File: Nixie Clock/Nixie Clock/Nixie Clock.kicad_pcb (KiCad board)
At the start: 2 copper layers, 4 parts, among them Q1 MPSA55, U1 MC34063AP

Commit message: More Nixie Stuff
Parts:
- added J1: PJ-202A, digikey-footprints:Barrel_Jack_5.5mmODx2.1mmID_PJ-202A, F.Cu at (107.2, 76.5)
- added S1: PEC11R-4215F-S0024, digikey-footprints:Rotary_Encoder_Switched_PEC11R, F.Cu at (112.5, 127.8)
- added SW1: 1825910-2, 1825910-2:TE_1825910-2, F.Cu at (83.9, 141.4)
- added U10: PIC16F15325-I/P, Package_DIP:DIP-14_W7.62mm, F.Cu at (159.0, 134.0)
- added U2: MC34063AP, Package_DIP:DIP-8_W7.62mm, F.Cu at (112.6, 91.6)
- added U3: IRF630, IRF630:TO220V, F.Cu at (95.8, 102.4)
- added U4: TPIC6595N, TPIC6595N:DIP254P762X508-20, F.Cu at (73.7, 102.4)
- added U5: TPIC6595N, TPIC6595N:DIP254P762X508-20, F.Cu at (53.1, 102.4)
- added U6: TPIC6595N, TPIC6595N:DIP254P762X508-20, F.Cu at (42.8, 102.4)
- added U7: TPIC6595N, TPIC6595N:DIP254P762X508-20, F.Cu at (84.0, 102.4)
- added U8: TPIC6595N, TPIC6595N:DIP254P762X508-20, F.Cu at (63.4, 102.4)
- added U9: TPIC6595N, TPIC6595N:DIP254P762X508-20, F.Cu at (72.7, 141.9)
- U1: value MC34063AP -> LM1086IT-5.0; footprint Package_DIP:DIP-8_W7.62mm -> LM1086IT-5:TO254P1054X470X1955-3
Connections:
- D1 pad 1: unconnected-(D1-Pad1) -> Net-(D1-Pad1)
- D1 pad 2: unconnected-(D1-Pad2) -> Net-(D1-Pad2)
- D2 pad 1: unconnected-(D2-Pad1) -> VDC
- D2 pad 2: unconnected-(D2-Pad2) -> Net-(D2-Pad2)
- Q1 pad 1: unconnected-(Q1-Pad1) -> Net-(D1-Pad1)
- Q1 pad 2: unconnected-(Q1-Pad2) -> Net-(D1-Pad2)
- Q1 pad 3: unconnected-(Q1-Pad3) -> GND

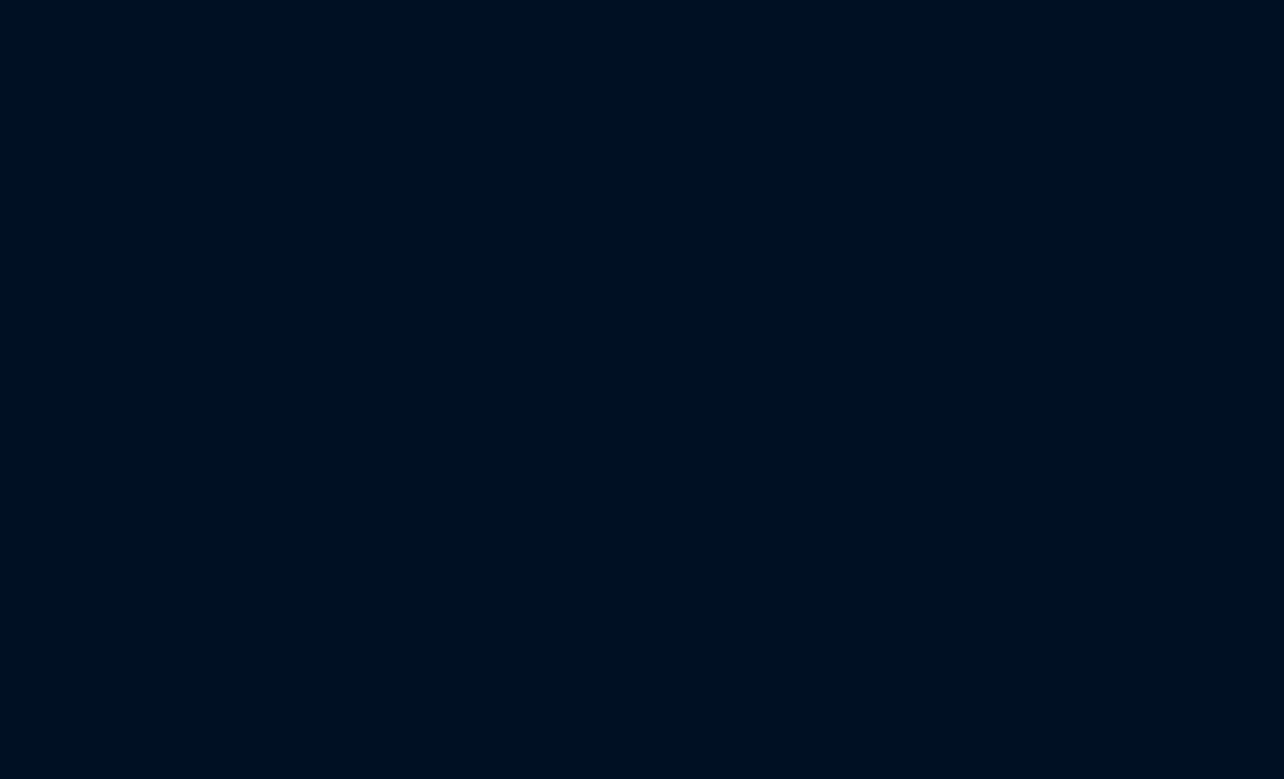
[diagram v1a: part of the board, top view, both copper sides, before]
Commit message: Need to add footprints for passives
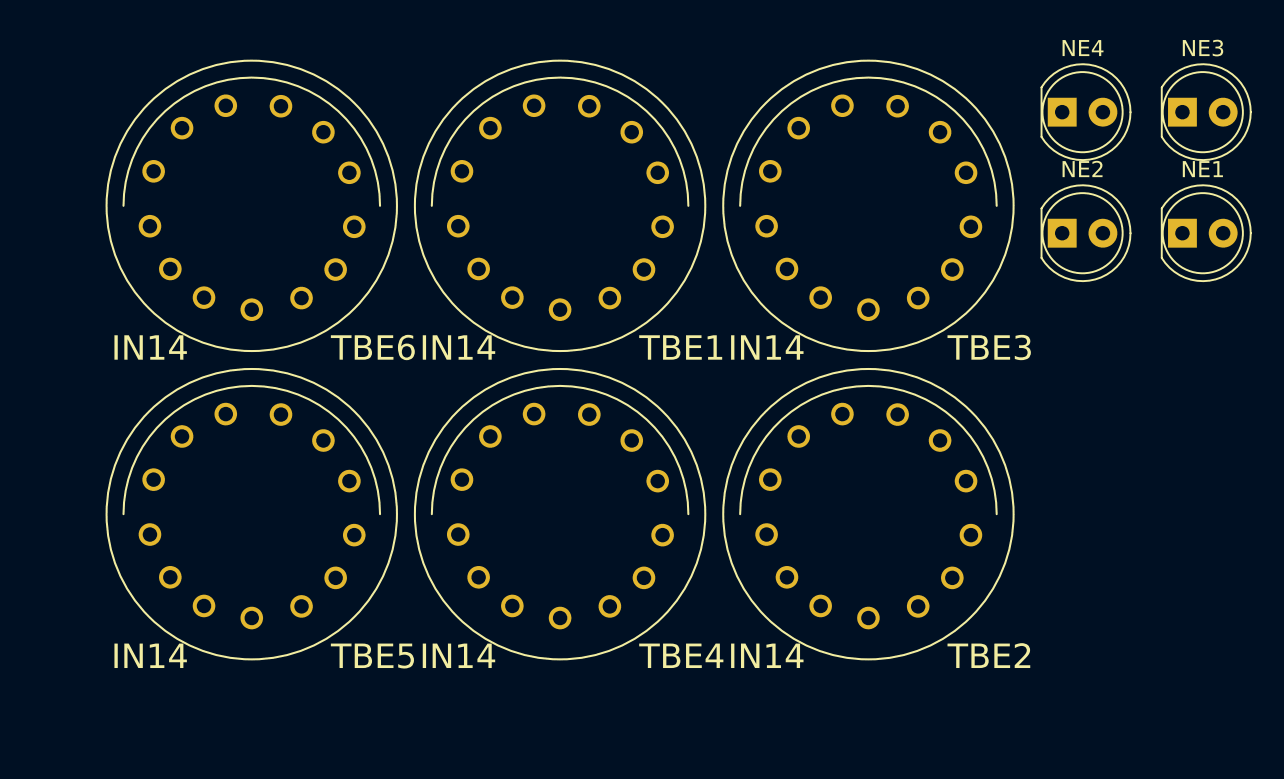
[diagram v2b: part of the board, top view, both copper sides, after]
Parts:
- added NE1: Lamp_Neon, LED_THT:LED_D5.0mm_Clear, F.Cu at (251.0, 53.0)
- added NE2: Lamp_Neon, LED_THT:LED_D5.0mm_Clear, F.Cu at (243.5, 53.0)
- added NE3: Lamp_Neon, LED_THT:LED_D5.0mm_Clear, F.Cu at (251.0, 45.5)
- added NE4: Lamp_Neon, LED_THT:LED_D5.0mm_Clear, F.Cu at (243.5, 45.5)
- added TBE1: IN14, tlnixie-master:IN-14-mod, F.Cu at (212.2, 51.3)
- added TBE2: IN14, tlnixie-master:IN-14-mod, F.Cu at (231.4, 70.5)
- added TBE3: IN14, tlnixie-master:IN-14-mod, F.Cu at (231.4, 51.3)
- added TBE4: IN14, tlnixie-master:IN-14-mod, F.Cu at (212.2, 70.5)
- added TBE5: IN14, tlnixie-master:IN-14-mod, F.Cu at (193.0, 70.5)
- added TBE6: IN14, tlnixie-master:IN-14-mod, F.Cu at (193.0, 51.3)
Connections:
- U1 pad 1: unconnected-(U1-Pad1) -> GND
- U1 pad 2: unconnected-(U1-Pad2) -> +5V
- U1 pad 3: unconnected-(U1-Pad3) -> +12V
- U9 pad 5: /Shift Registers/Tube_5_Digit_9 -> /Tube_5_Digit_9

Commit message: Started Routing
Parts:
- removed NE3, NE4: Lamp_Neon, LED_THT:LED_D5.0mm_Clear
- added C1: 10uF, Capacitor_THT:CP_Radial_D5.0mm_P2.00mm, F.Cu at (131.1, 57.1)
- added C10: 0.1uF, Capacitor_THT:C_Rect_L7.0mm_W3.5mm_P5.00mm, F.Cu at (147.1, 133.3)
- added C11: 0.1uF, Capacitor_THT:C_Rect_L7.0mm_W3.5mm_P5.00mm, F.Cu at (176.3, 133.4)
- added C12: 0.1uF, Capacitor_THT:C_Rect_L7.0mm_W3.5mm_P5.00mm, F.Cu at (197.9, 133.4)
- added C13: 18pF, Capacitor_THT:C_Rect_L7.0mm_W2.5mm_P5.00mm, F.Cu at (158.7, 58.8)
- added C14: 18pF, Capacitor_THT:C_Rect_L7.0mm_W2.5mm_P5.00mm, F.Cu at (158.7, 63.8)
- added C15: 0.1uF, Capacitor_THT:C_Rect_L7.0mm_W3.5mm_P5.00mm, F.Cu at (173.0, 51.0)
- added C16: 0.01uF, Capacitor_THT:C_Disc_D12.0mm_W4.4mm_P7.75mm, F.Cu at (198.2, 78.4)
- added C17: 0.01uF, Capacitor_THT:C_Disc_D12.0mm_W4.4mm_P7.75mm, F.Cu at (205.7, 78.4)
- added C18: 0.1uF, Capacitor_THT:C_Rect_L7.0mm_W3.5mm_P5.00mm, F.Cu at (191.7, 44.1)
- added C2: 10 uF, Capacitor_THT:CP_Radial_D5.0mm_P2.00mm, F.Cu at (137.3, 57.1)
- added C3: 680pF, Capacitor_THT:C_Disc_D7.5mm_W4.4mm_P5.00mm, F.Cu at (110.2, 52.7)
- added C4: 220uF 25V, Capacitor_THT:CP_Radial_D10.0mm_P5.00mm, F.Cu at (104.7, 74.7)
- added C5: 0.01uF, Capacitor_THT:C_Disc_D12.0mm_W4.4mm_P7.75mm, F.Cu at (116.5, 71.0)
- added C6: 2.2uF 250V, Capacitor_THT:CP_Radial_D6.3mm_P2.50mm, F.Cu at (84.7, 59.7)
- added C7: 0.1uF, Capacitor_THT:C_Rect_L7.0mm_W3.5mm_P5.00mm, F.Cu at (76.0, 133.4)
- added C8: 0.1uF, Capacitor_THT:C_Rect_L7.0mm_W3.5mm_P5.00mm, F.Cu at (97.6, 133.4)
- added C9: 0.1uF, Capacitor_THT:C_Rect_L7.0mm_W3.5mm_P5.00mm, F.Cu at (126.8, 133.4)
- added J2: Conn_01x05_Male, Connector_PinHeader_2.54mm:PinHeader_1x05_P2.54mm_Vertical, F.Cu at (184.9, 57.2)
- added L1: 150uH 1.1A, Inductor_THT:L_Radial_D12.0mm_P10.00mm_Neosid_SD12_style1, F.Cu at (98.7, 74.7)
- added R1: 0.5, Resistor_THT:R_Axial_DIN0207_L6.3mm_D2.5mm_P10.16mm_Horizontal, F.Cu at (125.7, 57.3)
- added R10: 10k, Resistor_THT:R_Axial_DIN0207_L6.3mm_D2.5mm_P10.16mm_Horizontal, F.Cu at (204.5, 72.1)
- added R11: 10k, Resistor_THT:R_Axial_DIN0207_L6.3mm_D2.5mm_P10.16mm_Horizontal, F.Cu at (199.4, 72.1)
- added R12: 10k, Resistor_THT:R_Axial_DIN0207_L6.3mm_D2.5mm_P10.16mm_Horizontal, F.Cu at (209.6, 61.9)
- added R13: 10k, Resistor_THT:R_Axial_DIN0207_L6.3mm_D2.5mm_P10.16mm_Horizontal, F.Cu at (181.6, 50.5)
- added R14: 14k, Resistor_THT:R_Axial_DIN0207_L6.3mm_D2.5mm_P10.16mm_Horizontal, F.Cu at (203.0, 108.0)
- added R15: 14k, Resistor_THT:R_Axial_DIN0207_L6.3mm_D2.5mm_P10.16mm_Horizontal, F.Cu at (131.6, 108.0)
- added R16: 14k, Resistor_THT:R_Axial_DIN0207_L6.3mm_D2.5mm_P10.16mm_Horizontal, F.Cu at (172.5, 100.3)
- added R17: 14k, Resistor_THT:R_Axial_DIN0207_L6.3mm_D2.5mm_P10.16mm_Horizontal, F.Cu at (121.7, 100.3)
- added R2: 0.5, Resistor_THT:R_Axial_DIN0207_L6.3mm_D2.5mm_P10.16mm_Horizontal, F.Cu at (120.7, 57.3)
- added R20: 14k, Resistor_THT:R_Axial_DIN0207_L6.3mm_D2.5mm_P10.16mm_Horizontal, F.Cu at (182.2, 108.0)
- added R21: 14k, Resistor_THT:R_Axial_DIN0207_L6.3mm_D2.5mm_P10.16mm_Horizontal, F.Cu at (101.8, 108.0)
- added R22: 14k, Resistor_THT:R_Axial_DIN0207_L6.3mm_D2.5mm_P10.16mm_Horizontal, F.Cu at (152.4, 108.0)
- added R23: 14k, Resistor_THT:R_Axial_DIN0207_L6.3mm_D2.5mm_P10.16mm_Horizontal, F.Cu at (81.1, 108.0)
- added R3: 1k, Resistor_THT:R_Axial_DIN0207_L6.3mm_D2.5mm_P10.16mm_Horizontal, F.Cu at (106.0, 53.7)
- added R4: 475k 1%, Resistor_THT:R_Axial_DIN0207_L6.3mm_D2.5mm_P10.16mm_Horizontal, F.Cu at (136.6, 80.2)
- added R5: 13.7k 1%, Resistor_THT:R_Axial_DIN0207_L6.3mm_D2.5mm_P10.16mm_Horizontal, F.Cu at (122.3, 70.0)
- added R6: 4.02k 1%, Resistor_THT:R_Axial_DIN0207_L6.3mm_D2.5mm_P10.16mm_Horizontal, F.Cu at (127.1, 80.2)
- added R7: 680 1%, Resistor_THT:R_Axial_DIN0207_L6.3mm_D2.5mm_P10.16mm_Horizontal, F.Cu at (131.8, 80.2)
- added R8: 10k, Resistor_THT:R_Axial_DIN0207_L6.3mm_D2.5mm_P10.16mm_Horizontal, F.Cu at (158.2, 72.3)
- added R9: 10k, Resistor_THT:R_Axial_DIN0207_L6.3mm_D2.5mm_P10.16mm_Horizontal, F.Cu at (194.3, 72.1)
- added REF**: Symbol_Highvoltage_Type1_CopperTop_Small, Symbol:Symbol_Highvoltage_Type1_CopperTop_Small, F.Cu at (80.3, 65.9)
- added Y1: 12.288MHz, Crystal:Crystal_HC49-4H_Vertical, F.Cu at (164.9, 58.9)
- moved U4 142.8 mm to (211.9, 138.4)
- moved U5 142.6 mm to (191.1, 138.4)
- moved NE2 129.2 mm to (120.5, 92.7)
- moved U6 123.8 mm to (161.3, 138.4)
- moved TBE6 114.6 mm to (86.1, 92.7)
- moved S1 114.2 mm to (196.3, 50.2)
- moved SW1 108.8 mm to (175.5, 82.8), turned to 180 degrees
- moved TBE4 107.6 mm to (106.9, 92.7)
- moved TBE2 97.3 mm to (136.7, 92.7)
- moved Q1 90.6 mm to (92.6, 59.9), turned to 90 degrees
- moved NE1 89.2 mm to (171.1, 92.7)
- moved U10 78.2 mm to (171.7, 56.9)
- moved D2 72.4 mm to (84.7, 64.9)
- moved U7 67.0 mm to (140.5, 138.4)
- moved D1 62.3 mm to (97.1, 58.3)
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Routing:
- net VDC: track 0.00 -> 132.4 mm
- net /Shift Clock: track 0.00 -> 127.2 mm
- net /Data Latch: track 0.00 -> 127.2 mm
- net /Tube_5_Digit_5: track 0.00 -> 51.3 mm
- net /Tube_5_Digit_4: track 0.00 -> 49.3 mm
- net /Tube_3_Digit_4: track 0.00 -> 49.3 mm, vias 0 -> 1
- net /Tube_1_Digit_4: track 0.00 -> 48.6 mm
- net /Tube_5_Digit_6: track 0.00 -> 48.3 mm, vias 0 -> 2
- net /Tube_3_Digit_5: track 0.00 -> 47.9 mm, vias 0 -> 1
- net /Tube_1_Digit_3: track 0.00 -> 47.2 mm
- net /Tube_4_Digit_5: track 0.00 -> 47.1 mm, vias 0 -> 1
- net /Tube_1_Digit_5: track 0.00 -> 47.0 mm, vias 0 -> 1
- net /Tube_5_Digit_3: track 0.00 -> 46.4 mm
- net /Tube_3_Digit_8: track 0.00 -> 46.1 mm
- net /Tube_3_Digit_3: track 0.00 -> 46.1 mm
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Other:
- board outline added: 150 x 104 mm

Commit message: Mostly finished Nixie Tube Project
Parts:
- moved C5 12.9 mm to (129.3, 69.7)
- moved D1 12.9 mm to (109.9, 57.0)
- moved J1 12.9 mm to (136.9, 49.6)
- moved R5 12.9 mm to (135.2, 68.7)
- moved R6 12.9 mm to (139.9, 78.9)
- moved C4 12.9 mm to (117.5, 73.4)
- moved U2 12.9 mm to (121.7, 57.2)
- moved C1 12.9 mm to (143.9, 55.8)
- moved C2 12.9 mm to (150.1, 55.8)
- moved C3 12.9 mm to (123.0, 51.4)
- moved C6 12.9 mm to (97.5, 58.4)
- moved Q1 12.9 mm to (105.4, 58.6)
- moved R1 12.9 mm to (138.5, 56.0)
- moved R2 12.9 mm to (133.5, 56.0)
- moved R3 12.9 mm to (118.9, 52.4)
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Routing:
- net +5V: track 38.2 -> 436.4 mm, vias 0 -> 3
- net VDC: track 132.4 -> 248.8 mm
- net /Data Output: track 0.00 -> 87.1 mm, vias 0 -> 1
- net /Shift Clock: track 127.2 -> 206.0 mm, vias 0 -> 1
- net /Data Latch: track 127.2 -> 202.0 mm, vias 0 -> 1
- net Net-(C4-Pad1): track 0.00 -> 47.3 mm
- net /Microcontroller/Encoder B: track 6.85 -> 44.7 mm
- net /Microcontroller/Rotary Button: track 0.00 -> 37.0 mm
- net +12V: track 0.28 -> 28.0 mm
- net Net-(C5-Pad1): track 0.03 -> 26.7 mm
- net /Microcontroller/Encoder A: track 7.98 -> 31.3 mm, vias 0 -> 1
- net Net-(D1-Pad2): track 0.00 -> 23.3 mm
- net Net-(D2-Pad2): track 0.76 -> 21.9 mm
- net Net-(D1-Pad1): track 0.00 -> 12.7 mm
- net Net-(C3-Pad1): track 0.00 -> 12.1 mm
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- added copper zone on B.Cu, net GND
- added copper zone on F.Cu, net GND
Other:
- board text added: "12V 2A Input"
- board text added: "Nixie Tube Clock"
- board text added: "Rotary Knob"
- board text added: "To set hours, push rotary knob and turn. Repeat for minutes and seconds. Push again to start clock."
- board text added: "WARNING! HIGH VOLTAGE!"

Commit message: Nixie
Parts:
- removed J2: Conn_01x05_Male, Connector_PinHeader_2.54mm:PinHeader_1x05_P2.54mm_Vertical
- removed R22, R23: 14k, Resistor_THT:R_Axial_DIN0207_L6.3mm_D2.5mm_P10.16mm_Horizontal
- removed REF**: Symbol_Highvoltage_Type1_CopperTop_Small, Symbol:Symbol_Highvoltage_Type1_CopperTop_Small
- added R18: 14k, Resistor_THT:R_Axial_DIN0204_L3.6mm_D1.6mm_P7.62mm_Horizontal, F.Cu at (243.5, 101.8)
- added R19: 14k, Resistor_THT:R_Axial_DIN0204_L3.6mm_D1.6mm_P7.62mm_Horizontal, F.Cu at (243.5, 98.7)
- C1, C2: footprint Capacitor_THT:CP_Radial_D5.0mm_P2.00mm -> Capacitor_THT:CP_Radial_D6.3mm_P2.50mm
- C10, C11, C12, C15, C18, C7, C8, C9: footprint Capacitor_THT:C_Rect_L7.0mm_W3.5mm_P5.00mm -> Capacitor_THT:CP_Radial_D4.0mm_P1.50mm
- C13, C14: footprint Capacitor_THT:C_Rect_L7.0mm_W2.5mm_P5.00mm -> Capacitor_THT:C_Disc_D5.0mm_W2.5mm_P2.50mm
- C16, C17, C5: footprint Capacitor_THT:C_Disc_D12.0mm_W4.4mm_P7.75mm -> Capacitor_THT:C_Disc_D5.1mm_W3.2mm_P5.00mm
- C3: footprint Capacitor_THT:C_Disc_D7.5mm_W4.4mm_P5.00mm -> Capacitor_THT:C_Disc_D3.8mm_W2.6mm_P2.50mm
- C4: footprint Capacitor_THT:CP_Radial_D10.0mm_P5.00mm -> Capacitor_THT:CP_Radial_D8.0mm_P3.50mm
- L1: footprint Inductor_THT:L_Radial_D12.0mm_P10.00mm_Neosid_SD12_style1 -> Inductor_THT:L_Radial_D21.0mm_P19.00mm
- R1, R2: footprint Resistor_THT:R_Axial_DIN0207_L6.3mm_D2.5mm_P10.16mm_Horizontal -> Resistor_THT:R_Axial_DIN0414_L11.9mm_D4.5mm_P15.24mm_Horizontal
- R10, R11, R12, R13, R8, R9: footprint Resistor_THT:R_Axial_DIN0207_L6.3mm_D2.5mm_P10.16mm_Horizontal -> Resistor_THT:R_Axial_DIN0309_L9.0mm_D3.2mm_P12.70mm_Horizontal
- R14, R15, R20, R21, R4, R6: footprint Resistor_THT:R_Axial_DIN0207_L6.3mm_D2.5mm_P10.16mm_Horizontal -> Resistor_THT:R_Axial_DIN0204_L3.6mm_D1.6mm_P7.62mm_Horizontal
- U3: footprint IRF630:TO220V -> Package_TO_SOT_THT:TO-220-3_Vertical
- moved U3 3.64 mm to (111.0, 62.9)
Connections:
- R11 pad 1: +5V -> Net-(R11-Pad1)
- R11 pad 2: Net-(R11-Pad2) -> +5V
- R12 pad 1: Net-(R10-Pad2) -> +5V
- R12 pad 2: +5V -> Net-(R10-Pad2)
- R13 pad 1: +5V -> /Microcontroller/Rotary Button
- R13 pad 2: /Microcontroller/Rotary Button -> +5V
- R9 pad 2: Net-(R11-Pad2) -> Net-(R11-Pad1)
- S1 pad A: Net-(R11-Pad2) -> Net-(R11-Pad1)
- TBE3 pad 1: Net-(R20-Pad1) -> Net-(R18-Pad1)
- TBE4 pad 1: Net-(R21-Pad1) -> Net-(R19-Pad1)
- TBE5 pad 1: Net-(R22-Pad1) -> Net-(R20-Pad1)
- TBE6 pad 1: Net-(R23-Pad1) -> Net-(R21-Pad1)
- U10 pad 12: /Microcontroller/Program Clock -> unconnected-(U10-Pad12)
- U10 pad 13: /Microcontroller/Program Data -> unconnected-(U10-Pad13)
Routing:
- net +5V: track 436.4 -> 0.00 mm, vias 3 -> 0
- net VDC: track 248.8 -> 0.00 mm
- net /Shift Clock: track 206.0 -> 0.00 mm, vias 1 -> 0
- net /Data Latch: track 202.0 -> 0.00 mm, vias 1 -> 0
- net /Data Output: track 87.1 -> 0.00 mm, vias 1 -> 0
- net /Tube_5_Digit_5: track 51.3 -> 0.00 mm
- net /Tube_5_Digit_4: track 49.3 -> 0.00 mm
- net /Tube_3_Digit_4: track 49.3 -> 0.00 mm, vias 1 -> 0
- net /Tube_1_Digit_4: track 48.6 -> 0.00 mm
- net /Tube_5_Digit_6: track 48.3 -> 0.00 mm, vias 2 -> 0
- net /Tube_3_Digit_5: track 47.9 -> 0.00 mm, vias 1 -> 0
- net Net-(C4-Pad1): track 47.3 -> 0.00 mm
- net /Tube_1_Digit_3: track 47.2 -> 0.00 mm
- net /Tube_4_Digit_5: track 47.1 -> 0.00 mm, vias 1 -> 0
- net /Tube_1_Digit_5: track 47.0 -> 0.00 mm, vias 1 -> 0
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- removed copper zone on B.Cu, net GND
- removed copper zone on F.Cu, net GND
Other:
- board outline removed

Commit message: Added additional parts
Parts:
- added D3: LED_RGB, CLY6D-FKC-CK1N1D1BB7D3D3:CLY6D-FKC-CK1N1D1BB7D3D3, F.Cu at (93.2, 107.3)
- added D4: LED_RGB, CLY6D-FKC-CK1N1D1BB7D3D3:CLY6D-FKC-CK1N1D1BB7D3D3, F.Cu at (113.9, 107.3)
- added D5: LED_RGB, CLY6D-FKC-CK1N1D1BB7D3D3:CLY6D-FKC-CK1N1D1BB7D3D3, F.Cu at (141.8, 107.3)
- added D6: LED_RGB, CLY6D-FKC-CK1N1D1BB7D3D3:CLY6D-FKC-CK1N1D1BB7D3D3, F.Cu at (162.6, 107.3)
- added D7: LED_RGB, CLY6D-FKC-CK1N1D1BB7D3D3:CLY6D-FKC-CK1N1D1BB7D3D3, F.Cu at (190.5, 107.3)
- added D8: LED_RGB, CLY6D-FKC-CK1N1D1BB7D3D3:CLY6D-FKC-CK1N1D1BB7D3D3, F.Cu at (211.2, 107.3)
- added H1: MountingHole, MountingHole:MountingHole_4.3mm_M4, F.Cu at (220.8, 50.0)
- added H2: MountingHole, MountingHole:MountingHole_4.3mm_M4, F.Cu at (80.0, 50.0)
- added H3: MountingHole, MountingHole:MountingHole_4.3mm_M4, F.Cu at (221.2, 147.5)
- added H4: MountingHole, MountingHole:MountingHole_4.3mm_M4, F.Cu at (80.0, 147.5)
- added R22: Resistor_THT:R_Axial_DIN0207_L6.3mm_D2.5mm_P10.16mm_Horizon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, Resistor_THT:R_Axial_DIN0207_L6.3mm_D2.5mm_P10.16mm_Horizontal, F.Cu at (81.0, 101.9)
- added R23: 110, Resistor_THT:R_Axial_DIN0411_L9.9mm_D3.6mm_P12.70mm_Horizontal, F.Cu at (102.3, 81.0)
- added R24: Resistor_THT:R_Axial_DIN0207_L6.3mm_D2.5mm_P10.16mm_Horizon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, Resistor_THT:R_Axial_DIN0207_L6.3mm_D2.5mm_P10.16mm_Horizontal, F.Cu at (81.0, 128.0)
- added R25: 150, Resistor_THT:R_Axial_DIN0414_L11.9mm_D4.5mm_P15.24mm_Horizontal, F.Cu at (104.6, 94.0)
- added R26: Resistor_THT:R_Axial_DIN0207_L6.3mm_D2.5mm_P10.16mm_Horizon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, Resistor_THT:R_Axial_DIN0207_L6.3mm_D2.5mm_P10.16mm_Horizontal, F.Cu at (81.0, 114.9)
- added R27: 150, Resistor_THT:R_Axial_DIN0414_L11.9mm_D4.5mm_P15.24mm_Horizontal, F.Cu at (104.6, 87.0)
- added RV1: 10K, WH148:WH148, F.Cu at (81.0, 61.2)
- added RV2: 10K, WH148:WH148, F.Cu at (81.0, 93.2)
- added RV3: 10K, WH148:WH148, F.Cu at (81.0, 77.2)
- Q1: footprint MPSA55:TO92127P520H787-3 -> Package_TO_SOT_THT:TO-92_Inline
- moved R19 128.1 mm to (117.2, 119.8)
- moved R18 52.9 mm to (193.7, 119.8)
- moved C15 43.0 mm to (210.5, 72.0), turned to 90 degrees
- moved C18 39.4 mm to (210.5, 78.8), turned to 90 degrees
- moved R12 37.8 mm to (177.0, 81.1), turned to 90 degrees
- moved R9 36.5 mm to (159.0, 81.1)
- moved C17 35.0 mm to (171.5, 85.8)
- moved R10 34.7 mm to (171.0, 81.1)
- moved R11 34.6 mm to (165.0, 68.4), turned to -90 degrees
- moved S1 34.5 mm to (162.3, 56.5)
- moved C16 34.4 mm to (164.5, 85.8)
- moved R2 33.6 mm to (145.8, 87.2), turned to 90 degrees
- moved Q1 33.3 mm to (119.2, 88.9), turned to 0 degrees
- moved C2 32.3 mm to (152.2, 88.1), turned to -90 degrees
- moved R1 31.3 mm to (138.8, 87.2), turned to 90 degrees
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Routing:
- net +5V: track 0.00 -> 376.8 mm, vias 0 -> 6
- net VDC: track 0.00 -> 207.1 mm, vias 0 -> 1
- net /Shift Clock: track 0.00 -> 193.7 mm, vias 0 -> 1
- net /Data Latch: track 0.00 -> 188.6 mm, vias 0 -> 1
- net /LEDS/RED: track 0.00 -> 178.8 mm, vias 0 -> 2
- net /LEDS/GRN: track 0.00 -> 160.9 mm, vias 0 -> 12
- net /LEDS/BLU: track 0.00 -> 150.9 mm
- net +12V: track 0.00 -> 109.7 mm
- net Net-(R22-Pad1): track 0.00 -> 71.0 mm
- net /Microcontroller/Rotary Button: track 0.00 -> 66.0 mm
- net Net-(R26-Pad1): track 0.00 -> 63.5 mm, vias 0 -> 1
- net /Tube_3_Digit_9: track 0.00 -> 57.8 mm, vias 0 -> 2
- net /Tube_1_Digit_9: track 0.00 -> 55.4 mm, vias 0 -> 2
- net Net-(R24-Pad1): track 0.00 -> 51.6 mm
- net /Data Output: track 0.00 -> 50.6 mm, vias 0 -> 2
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- added copper zone on B.Cu, net GND
- added copper zone on F.Cu, net GND
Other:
- board outline added: 151.2 x 108 mm
- board text added: "5V REGULATOR"
- board text added: "BLUE"
- board text added: "GREEN"
- board text added: "HOT!"
- board text added: "MICROCONTROLLER"
- board text added: "Push knob to adjust hours Repeat for minutes and seconds Push again to return to normal"
- board text added: "RED"
- board text added: "RESET"
- board text removed: "To set hours, push rotary knob and turn. Repeat for minutes and seconds. Push again to start clock."
